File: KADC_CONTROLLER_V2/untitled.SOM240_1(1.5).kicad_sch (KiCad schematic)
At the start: 24 parts, among them J10 ADM6-60-01.5-L-4-2-A-TR, J7 1766453, SW2 SW_MEC_5G

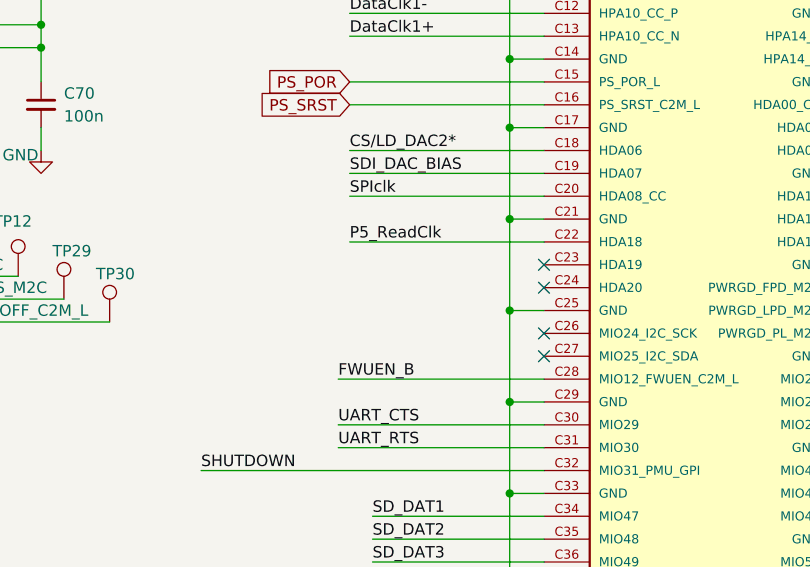
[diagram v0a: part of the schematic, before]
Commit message: Many Updates
Starting new power sequence and implementing KR260 PS circuitry.
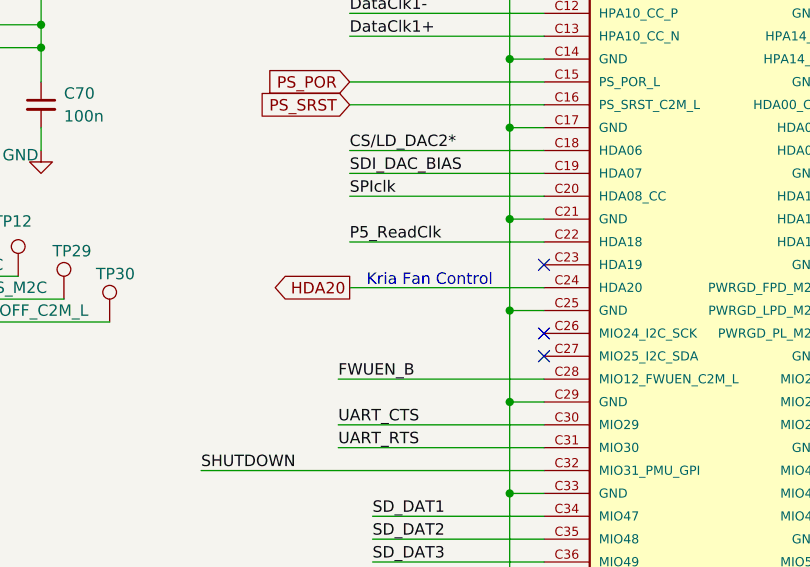
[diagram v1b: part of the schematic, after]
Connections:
- net HDA20: now reaches J10.C24 (HDA20)
- no-connect marks 61 -> 60
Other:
- note added: "Kria Fan Control"
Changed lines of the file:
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@@
 		)
 	)
+	(text "Kria Fan Control"
+		(exclude_from_sim no)
+		(at 201.93 80.518 0)
+		(effects
+			(font
+				(size 1.27 1.27)
+			)
+		)
+	)
 	(text "From Kria"
 		(exclude_from_sim no)
@@
 	)
 	(no_connect
-		(at 214.63 81.28)
-	)
-	(no_connect
 		(at 214.63 162.56)
 	)
@@
 	(wire
 		(pts
+			(xy 193.04 81.28) (xy 214.63 81.28)
+		)
+		(stroke
+			(width 0)
+			(type default)
+		)
+	)
+	(wire
+		(pts
 			(xy 60.96 36.83) (xy 80.01 36.83)
 		)
@@
 			)
 		)
+	)
+	(global_label "HDA20"
+		(shape output)
+		(at 193.04 81.28 180)
+		(fields_autoplaced yes)
+		(effects
+			(font
+				(size 1.27 1.27)
+			)
+			(justify right)
+		)
+		(property "Intersheetrefs" "${INTERSHEET_REFS}"
+			(at 183.9467 81.28 0)
+			(hide yes)
+			(show_name no)
+			(do_not_autoplace no)
+			(effects
+				(font
+					(size 1.27 1.27)
+				)
+				(justify right)
+			)
+		)
